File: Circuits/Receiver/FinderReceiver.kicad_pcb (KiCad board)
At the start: 2 copper layers, 59 x 28 mm, 9 parts, among them P1 WRITER-VCC, SW1 SW_PUSH, U1 TWE_LITE_SMD, U2 NJU72501MJE

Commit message: Artwork in progress.
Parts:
- moved R1 2.12 mm to (28.5, 25.5)
- moved U1 0.25 mm to (52.5, 31.8)
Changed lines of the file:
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@@
     (links 31)
     (no_connects 31)
-    (area 13.670999 15.246 73.329001 51.435)
+    (area 0 0 0 0)
     (thickness 1)
     (drawings 3)
@@
   )
   (module Resistors_SMD:R_0603 (layer F.Cu)
-    (at 27 24 270)
+    (at 28.5 25.5 270)
     (descr "Resistor SMD 0603, reflow soldering, Vishay (see dcrcw.pdf)")
     (tags "resistor 0603")
@@
   )
   (module favorites:TWE-001L-NC7 (layer F.Cu)
-    (at 52.5 32 90)
+    (at 52.451 31.75 90)
     (descr http://www.tocos-wireless.com/files/datasheet/TWD-PDS-TWE001L-JP-1.30.pdf)
     (fp_text reference U1 (at 0 -8.255 90) (layer F.SilkS)
@@
       )
     )
+  )
+  (zone (net 0) (net_name "") (layer F.Cu) (hatch edge 0.508)
+    (connect_pads (clearance 0.508))
+    (min_thickness 0.254)
+    (keepout (tracks allowed) (vias not_allowed) (copperpour allowed))
+    (fill (arc_segments 16) (thermal_gap 0.508) (thermal_bridge_width 0.508))
+    (polygon
+      (pts
+        (xy 45.466 24.765) (xy 45.466 26.543) (xy 46.736 26.543) (xy 46.736 33.02) (xy 49.149 33.02)
+        (xy 49.149 37.465) (xy 57.658 37.465) (xy 57.658 38.735) (xy 59.436 38.735) (xy 59.436 36.957)
+        (xy 58.166 36.957) (xy 58.166 26.543) (xy 59.436 26.543) (xy 59.436 24.765) (xy 57.658 24.765)
+        (xy 57.658 26.035) (xy 47.244 26.035) (xy 47.244 24.765)
+      )
+    )
+  )
+  (zone (net 0) (net_name "") (layer F.Cu) (hatch edge 0.508)
+    (connect_pads (clearance 0.508))
+    (min_thickness 0.254)
+    (keepout (tracks not_allowed) (vias not_allowed) (copperpour allowed))
+    (fill (arc_segments 16) (thermal_gap 0.508) (thermal_bridge_width 0.508))
+    (polygon
+      (pts
+        (xy 28.3 28.3) (xy 31.7 28.3) (xy 31.7 31.8) (xy 28.3 31.8)
+      )
+    )
+  )
+  (zone (net 0) (net_name "") (layer B.Cu) (hatch edge 0.508)
+    (connect_pads (clearance 0.508))
+    (min_thickness 0.254)
+    (keepout (tracks not_allowed) (vias not_allowed) (copperpour allowed))
+    (fill (arc_segments 16) (thermal_gap 0.508) (thermal_bridge_width 0.508))
+    (polygon
+      (pts
+        (xy 28.3 28.3) (xy 28.3 31.8) (xy 31.7 31.8) (xy 31.7 28.3)
+      )
+    )

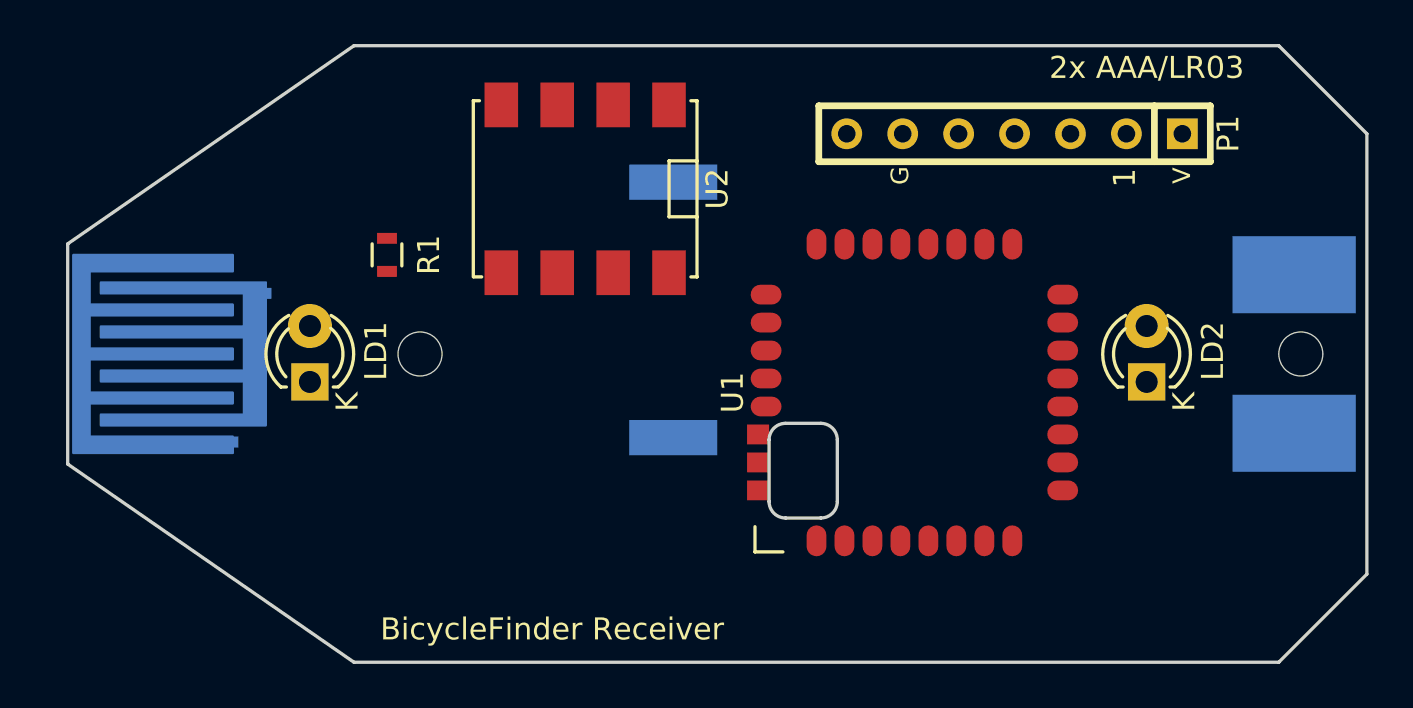
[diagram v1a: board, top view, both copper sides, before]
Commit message: Shrunk rubber switch pattern.
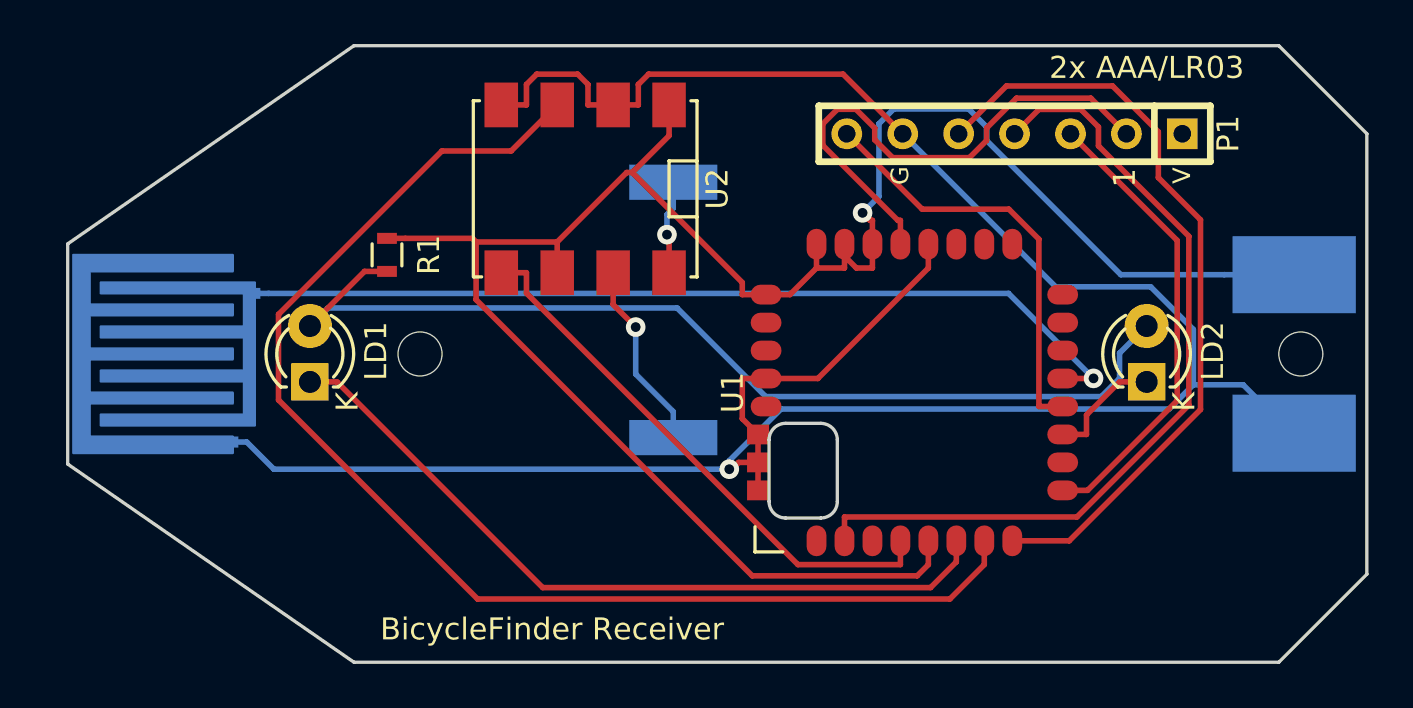
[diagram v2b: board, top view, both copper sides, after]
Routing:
- net GND: track 0.00 -> 112.0 mm, vias 0 -> 1
- net VCC: track 0.00 -> 93.5 mm, vias 0 -> 1
- net /SOUND: track 0.00 -> 58.0 mm
- net /LED: track 0.00 -> 46.5 mm
- net /DI1: track 0.00 -> 41.1 mm, vias 0 -> 1
- net /PRG: track 0.00 -> 37.8 mm
- net /TXD: track 0.00 -> 35.3 mm
- net /DO3: track 0.00 -> 34.7 mm
- net /EN2: track 0.00 -> 25.2 mm
- net /RST: track 0.00 -> 24.4 mm
- net /RXD: track 0.00 -> 21.0 mm
- net /CFG: track 0.00 -> 19.4 mm
- net /VO2: track 0.00 -> 8.62 mm, vias 0 -> 1
- net /DO4: track 0.00 -> 5.32 mm
- net /VO1: track 0.00 -> 4.27 mm, vias 0 -> 1

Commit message: Changed location of parts.
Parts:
- moved SP1 2.06 mm to (39.5, 27.5)
- moved U2 1.58 mm to (38.0, 24.0)
- moved U1 0.60 mm to (53.0, 32.0)
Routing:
- net /PRG: track 37.8 -> 22.8 mm
- net /DI1: track 41.1 -> 52.7 mm
- net /RST: track 24.4 -> 14.1 mm
- net GND: track 112.0 -> 105.7 mm
- net /LED: track 46.5 -> 51.4 mm
- net /VO2: track 8.62 -> 5.59 mm
- net /VO1: track 4.27 -> 7.07 mm
- net VCC: track 93.5 -> 91.4 mm
- net /DO3: track 34.7 -> 35.4 mm
- net /TXD: track 35.3 -> 34.6 mm
- net /CFG: track 19.4 -> 18.7 mm, vias 0 -> 1

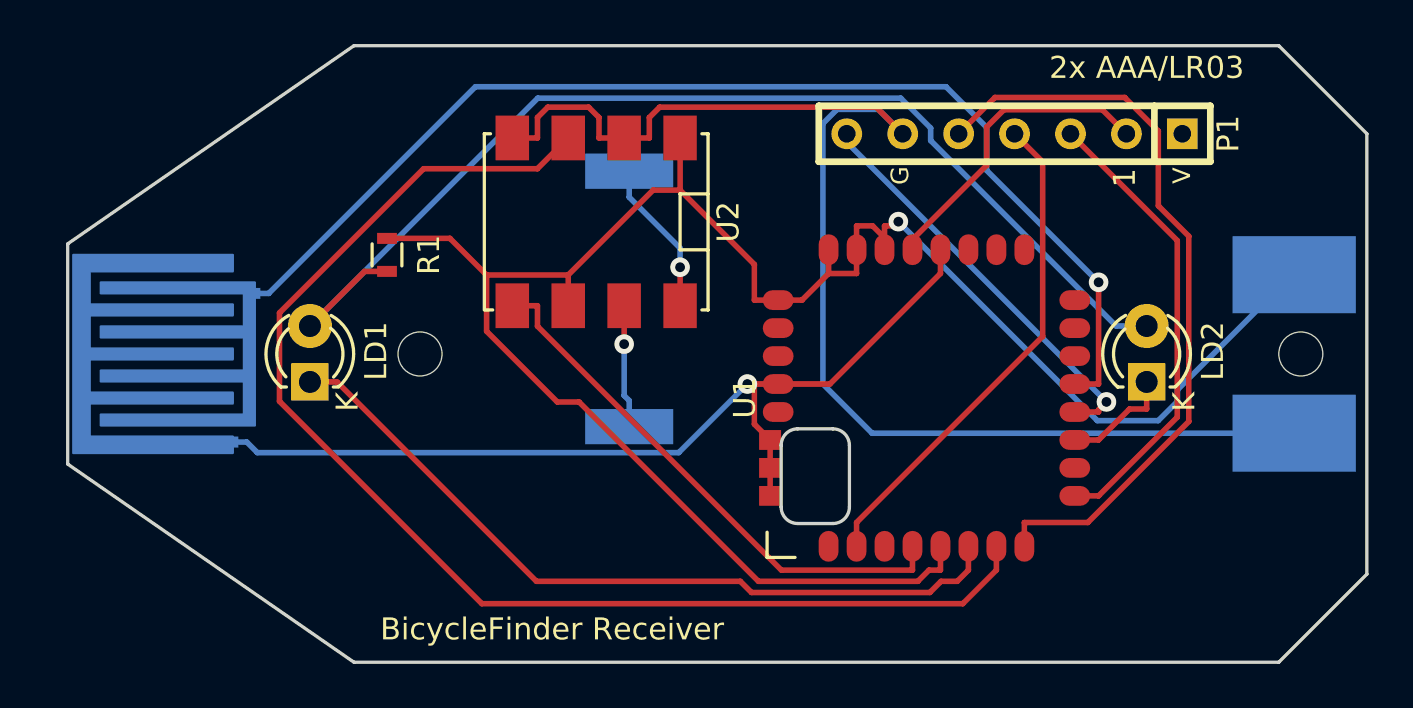
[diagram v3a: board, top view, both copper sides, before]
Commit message: Replaced outline edge.
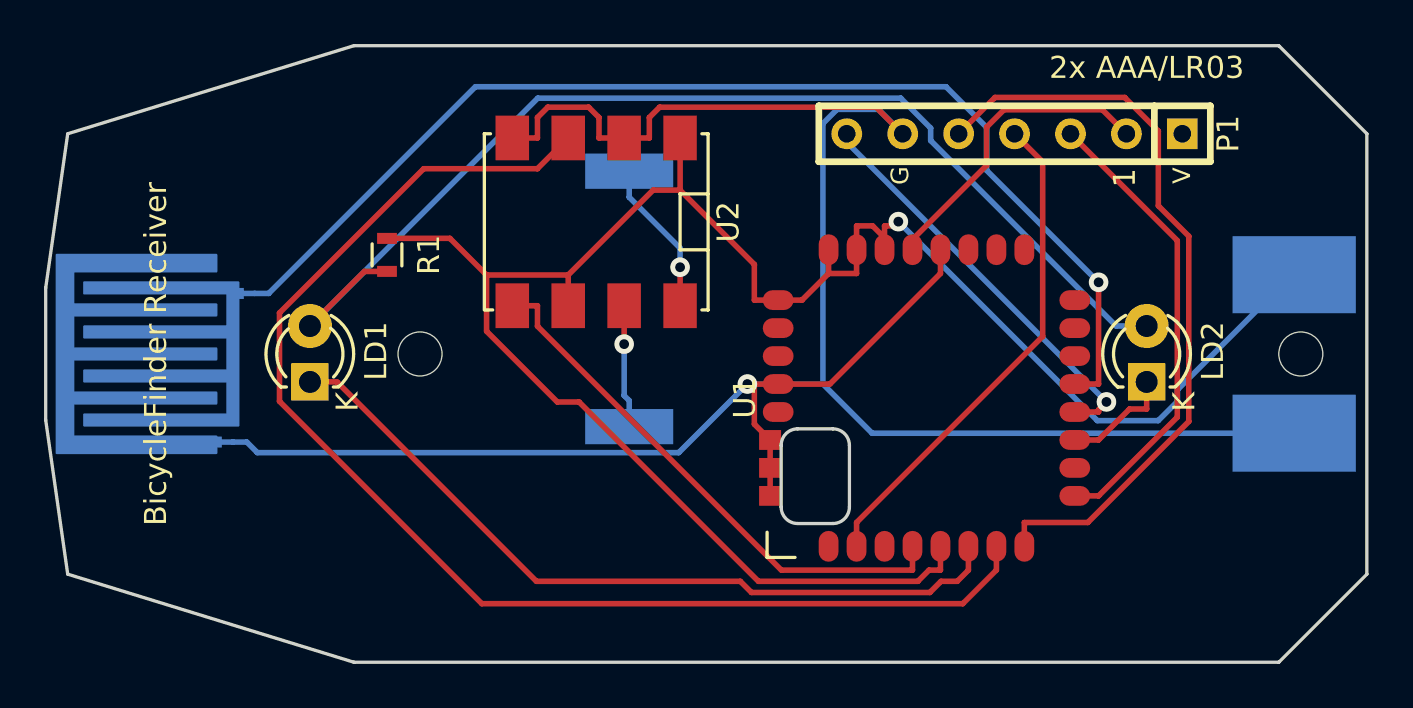
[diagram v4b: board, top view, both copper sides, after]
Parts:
- moved SW1 0.75 mm to (17.8, 30.0)
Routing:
- net GND: track 105.7 -> 106.4 mm
- net /DI1: track 52.7 -> 53.5 mm
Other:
- board size 59 x 28 mm -> 60 x 28 mm

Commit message: Connect DO1 to EN1.
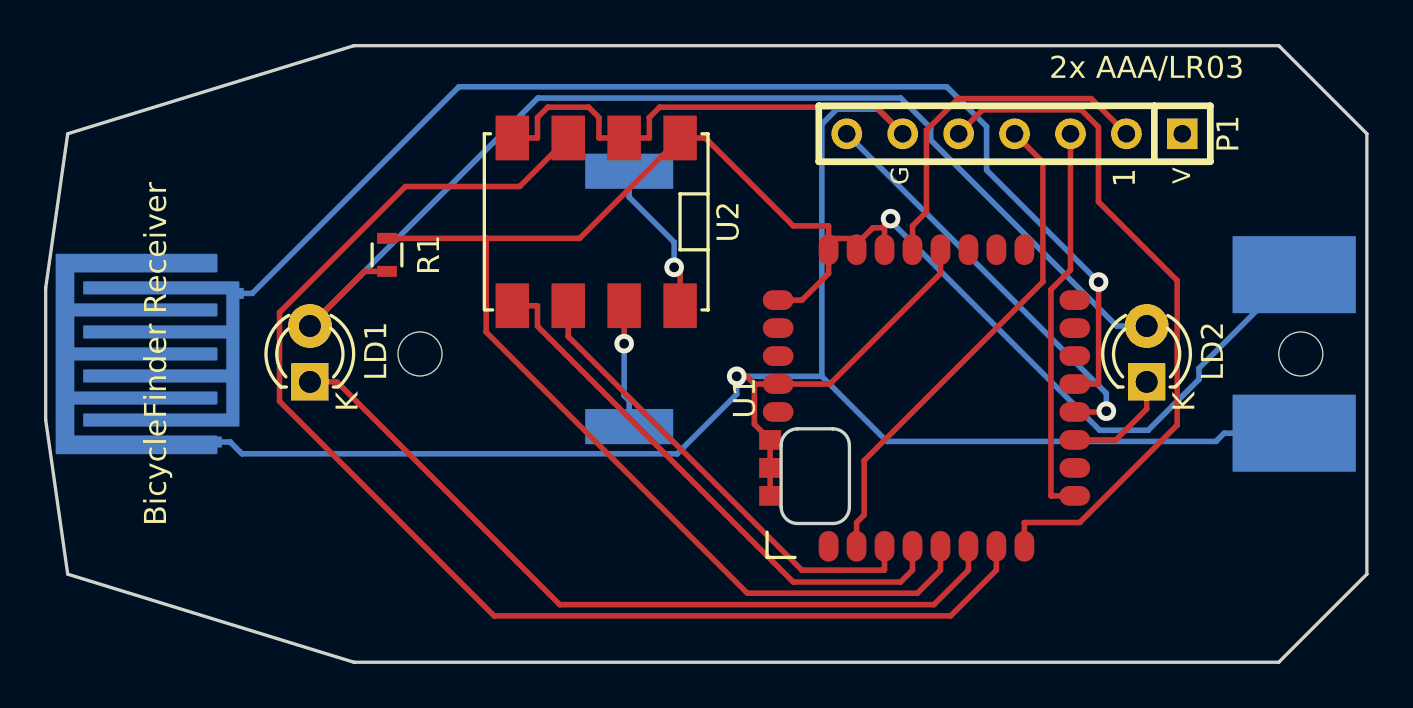
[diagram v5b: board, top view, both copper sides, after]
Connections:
- U1 pad 3: Net-(U1-Pad3) -> /EN1
- U2 pad 6: VCC -> /EN1
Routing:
- net /EN1: track 0.00 -> 21.2 mm
- net /RXD: track 21.0 -> 17.9 mm
- net /TXD: track 34.6 -> 32.0 mm
- net /RST: track 14.1 -> 16.0 mm
- net GND: track 106.4 -> 107.9 mm
- net VCC: track 91.4 -> 90.3 mm

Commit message: Added pull down registers.
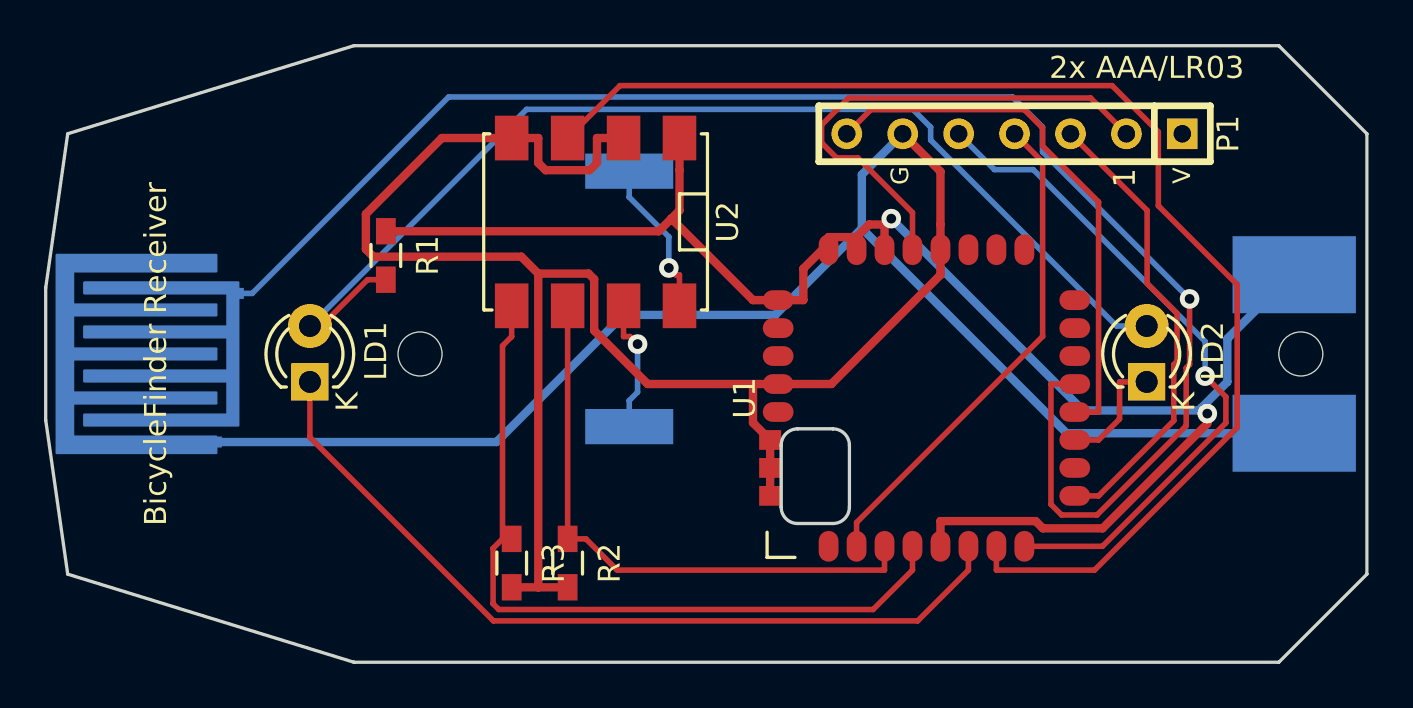
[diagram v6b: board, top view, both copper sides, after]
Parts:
- added R2: 2M, Resistors_SMD:R_0603_HandSoldering, F.Cu at (36.7, 39.5)
- added R3: 2M, Resistors_SMD:R_0603_HandSoldering, F.Cu at (34.2, 39.5)
- R1: footprint Resistors_SMD:R_0603 -> Resistors_SMD:R_0603_HandSoldering
- moved R1 0.06 mm to (28.4, 25.5)
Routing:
- net GND: track 107.9 -> 140.5 mm, vias 1 -> 0
- net /DI1: track 53.5 -> 71.7 mm
- net VCC: track 90.3 -> 74.9 mm, vias 1 -> 2
- net /EN2: track 25.2 -> 35.3 mm
- net /RST: track 16.0 -> 23.0 mm
- net /CFG: track 18.9 -> 24.7 mm, vias 1 -> 0
- net /EN1: track 21.2 -> 26.6 mm
- net /RXD: track 17.9 -> 21.0 mm
- net /DO3: track 35.8 -> 37.9 mm
- net /TXD: track 32.0 -> 30.7 mm, vias 0 -> 1
- net /SOUND: track 59.0 -> 58.3 mm
- net /LED: track 51.4 -> 50.8 mm
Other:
- net class Power: trace_width 0.508 -> 0.381
